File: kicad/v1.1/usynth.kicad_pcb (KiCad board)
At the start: 2 copper layers, 40 x 30 mm, 54 parts, among them J1 MAIN_CONN, J2 AVR-ISP-6, J3 LINE_OUT, J4 MIDI_IN, U1 ATmega328-AU, U2 MCP4921, U3 TL431DBZ, U4 MCP6001, U5 6N137, U6 L78L05_SO8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

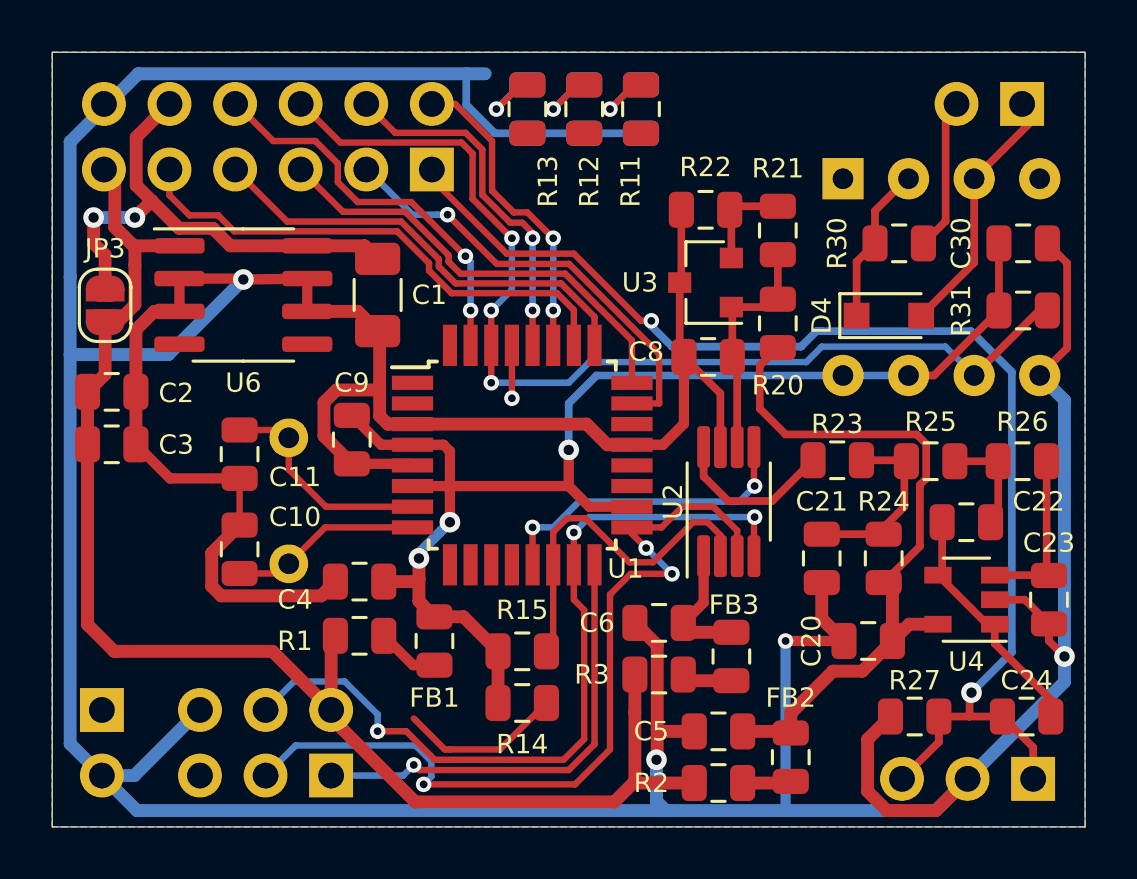
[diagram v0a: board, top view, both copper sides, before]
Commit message: All traces are connected
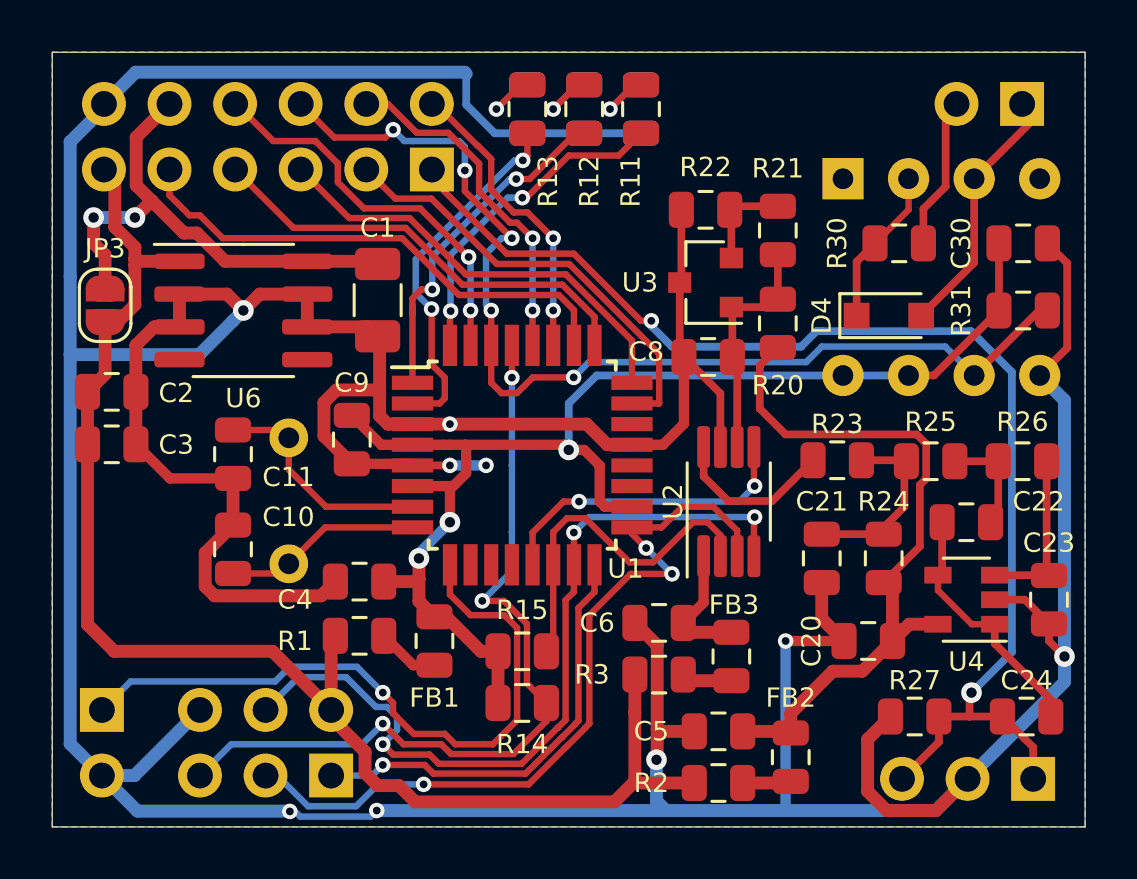
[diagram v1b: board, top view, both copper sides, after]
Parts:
- moved U6 0.60 mm to (127.4, 70.0)
- moved C10 0.25 mm to (127.0, 79.2)
- moved C11 0.25 mm to (127.0, 75.6)
- moved C1 0.20 mm to (132.6, 69.6)
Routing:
- net /SEL_2: track 0.00 -> 26.8 mm, vias 0 -> 1
- net /RESET: track 8.43 -> 31.8 mm, vias 1 -> 3
- net /LED_3: track 0.00 -> 14.0 mm, vias 0 -> 2
- net /LED_2: track 0.00 -> 13.6 mm, vias 0 -> 2
- net /LED_1: track 0.00 -> 12.8 mm, vias 0 -> 2
- net /SCK: track 32.9 -> 30.6 mm
- net GND: track 221.4 -> 223.3 mm, vias 4 -> 9
- net /RX: track 40.8 -> 41.9 mm, vias 3 -> 5
- net Net-(C1-Pad2): track 20.7 -> 19.8 mm
- net /MISO: track 17.8 -> 17.0 mm
- net +5VD: track 50.7 -> 51.3 mm
- net +5V: track 56.1 -> 55.6 mm
- net /ADC0: track 17.1 -> 17.3 mm, vias 1 -> 0
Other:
- board text added: "µsynth v1.1 Jacek Wieczorek 09.2020"
- board text removed: "ADC"
- board text removed: "SEL 0 1 2"
- board text removed: "µsynth v1.0 Jacek Wieczorek 01.2020"

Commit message: The PCB is finished (probably)
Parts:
- moved C5 0.20 mm to (145.8, 86.5)
- moved FB2 0.20 mm to (148.6, 87.5)
- moved R2 0.20 mm to (145.8, 88.5)
- moved U3 0.10 mm to (145.2, 68.9)
- moved R20 0.10 mm to (148.2, 70.5)
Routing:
- net GND: track 223.3 -> 380.8 mm, vias 9 -> 71
- net /VREF: track 9.16 -> 11.4 mm
- net /+5VA: track 27.9 -> 26.5 mm
- net /SCL: track 13.6 -> 14.8 mm
- net /SDA: track 11.7 -> 12.8 mm
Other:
- board text added: "MIDI IN"

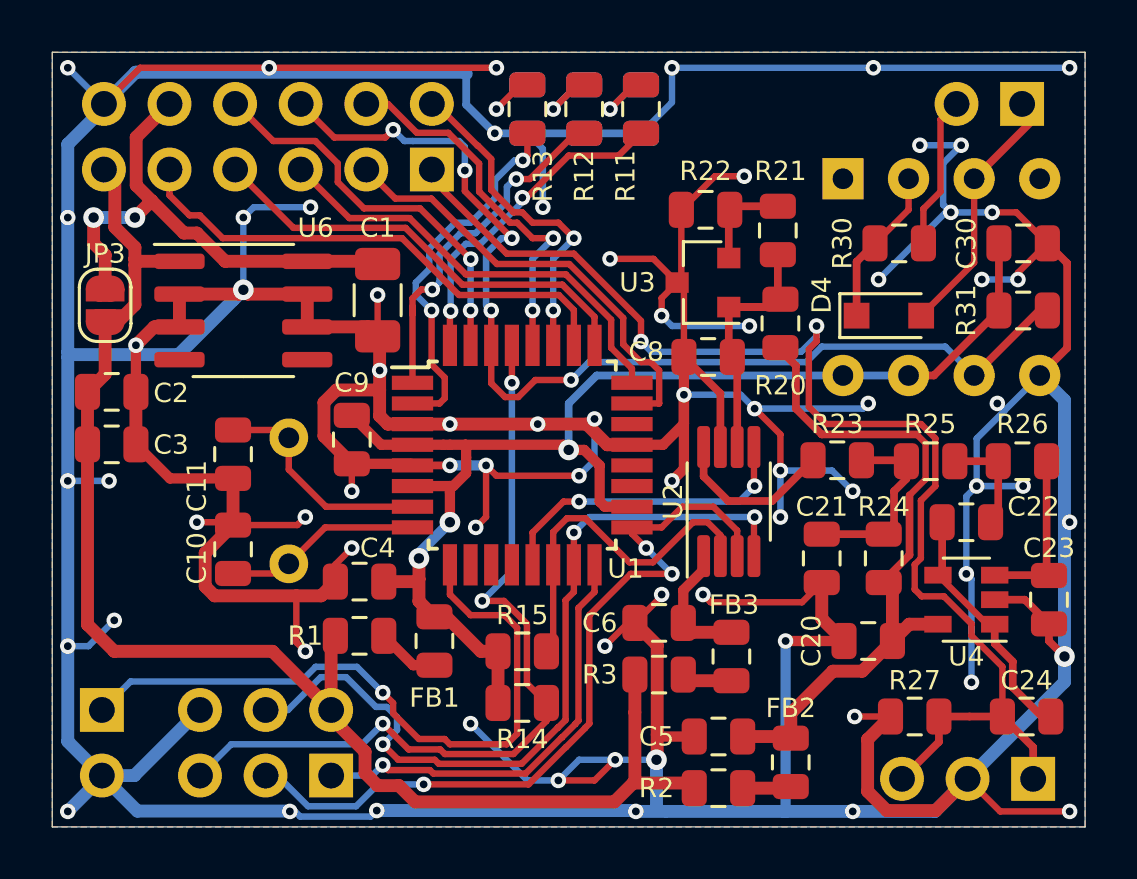
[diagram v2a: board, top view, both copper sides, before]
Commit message: Export gerber files, add PCB version suitable for JLC PCB SMT assembly
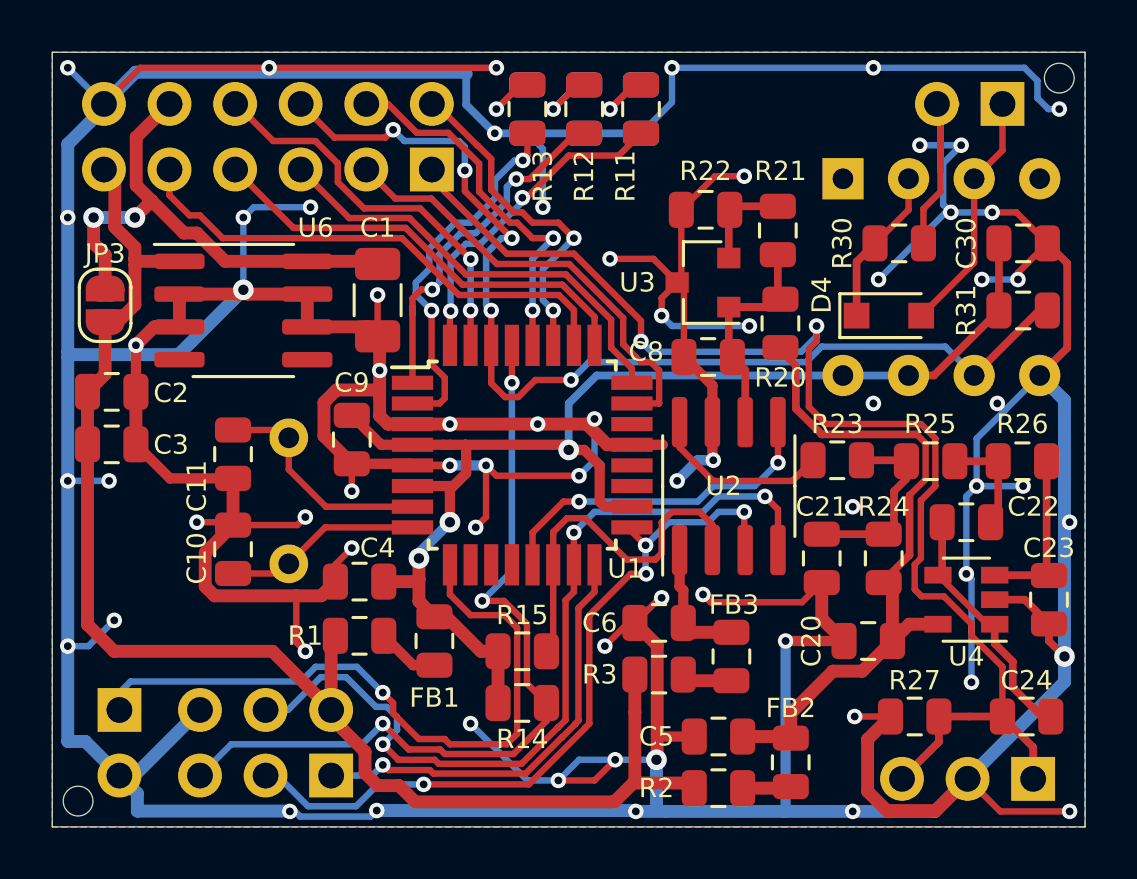
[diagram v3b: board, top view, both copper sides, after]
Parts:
- added REF**: JLCPCB_Tooling, usynth:JLCPCB_Tooling, F.Cu at (121.0, 89.0)
- added REF**: JLCPCB_Tooling, usynth:JLCPCB_Tooling, F.Cu at (159.0, 61.0)
- U2: footprint Package_SO:MSOP-8_3x3mm_P0.65mm -> Package_SO:SOIC-8_3.9x4.9mm_P1.27mm
- moved J4 0.76 mm to (156.8, 62.0)
- moved JP2 0.68 mm to (122.6, 85.5)
- moved U2 0.60 mm to (146.2, 76.8)
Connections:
- U1 pad 10: (no net) -> Net-(U1-Pad10)
- U1 pad 11: (no net) -> Net-(U1-Pad11)
- U1 pad 12: (no net) -> Net-(U1-Pad12)
- U1 pad 19: (no net) -> Net-(U1-Pad19)
- U1 pad 20: (no net) -> Net-(U1-Pad20)
- U1 pad 22: (no net) -> Net-(U1-Pad22)
- U5 pad 1: (no net) -> Net-(U5-Pad1)
- U6 pad 4: (no net) -> Net-(U6-Pad4)
- U6 pad 5: (no net) -> Net-(U6-Pad5)
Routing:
- net GND: track 380.8 -> 358.9 mm, vias 71 -> 67
- net Net-(J4-Pad2): track 5.94 -> 8.60 mm
- net /MOSI: track 31.6 -> 33.3 mm
- net /SCK: track 30.6 -> 29.3 mm, vias 3 -> 4
- net /~LDAC: track 12.2 -> 13.4 mm
- net Net-(D4-Pad2): track 10.1 -> 9.50 mm
- net /~CS: track 13.8 -> 14.4 mm
- net /DAC_OUT: track 6.42 -> 7.01 mm
- net /VREF: track 11.4 -> 10.9 mm
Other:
- board text added: "µsynth v1.1c Jacek Wieczorek 09.2020"
- board text removed: "µsynth v1.1 Jacek Wieczorek 09.2020"
